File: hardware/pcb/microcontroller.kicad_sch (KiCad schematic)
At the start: 16 parts, among them U4 STM32G474CBT6TR, Y1 CS10820-24M

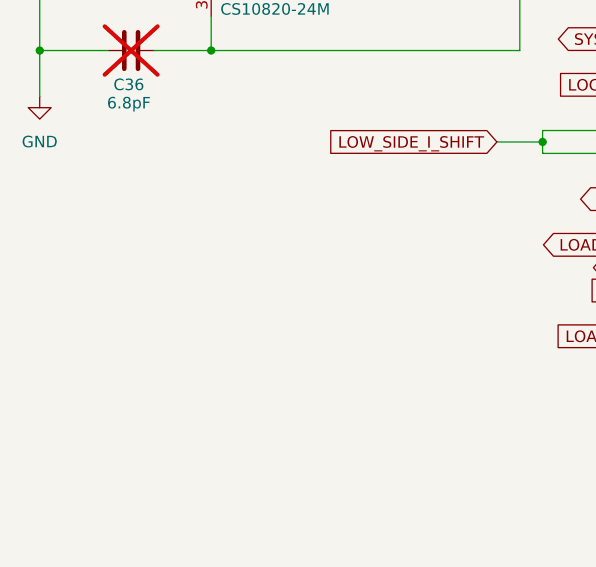
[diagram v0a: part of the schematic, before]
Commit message: Add TPS48110 disconnect, OVP, and discharge design; update MCU and power schematics
Documents the buck high-side short-circuit fault, programmable output
overvoltage protection, and controlled output discharge, and records the
saved schematic changes.

Co-Authored-By: Claude Opus 5.5 <noreply@anthropic.com>
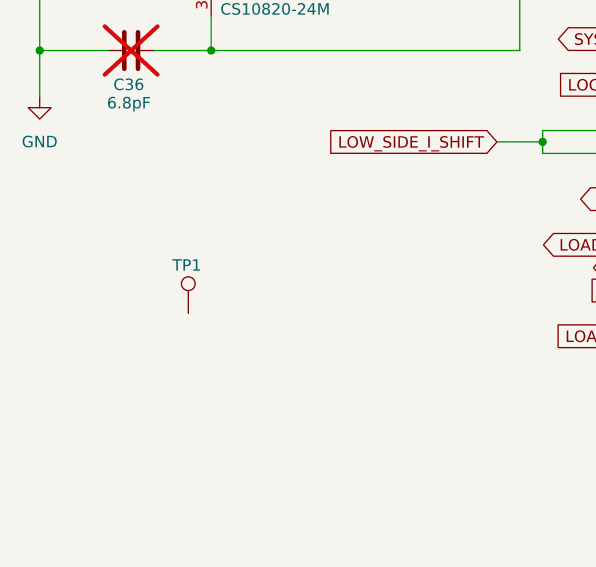
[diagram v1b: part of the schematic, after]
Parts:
- added TP1: TestPoint, verified:P-00046_PCB, symbol verified:P-00046
